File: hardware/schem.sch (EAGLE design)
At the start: 18 parts, among them IC1 7805L, IC2 L298, U2 TINY85-20-DIP

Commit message: Improved ground plane
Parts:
- TINY85: value TINY85-20-DIP -> TINY85
- renumbered U2 to TINY85
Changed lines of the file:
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@@
 <part name="P+4" library="supply1" deviceset="+5V" device=""/>
 <part name="GND2" library="supply1" deviceset="GND" device=""/>
-<part name="U2" library="SparkFun-DigitalIC" deviceset="ATTINY45" device="TINY85-20-DIP" value="TINY85-20-DIP"/>
+<part name="TINY85" library="SparkFun-DigitalIC" deviceset="ATTINY45" device="TINY85-20-DIP" value="TINY85"/>
 <part name="GND4" library="supply1" deviceset="GND" device=""/>
 <part name="P+5" library="supply1" deviceset="+5V" device=""/>
@@
 <instance part="P+4" gate="1" x="180.34" y="106.68"/>
 <instance part="GND2" gate="1" x="165.1" y="86.36"/>
-<instance part="U2" gate="G$1" x="73.66" y="43.18"/>
+<instance part="TINY85" gate="G$1" x="73.66" y="43.18"/>
 <instance part="GND4" gate="1" x="111.76" y="86.36"/>
 <instance part="P+5" gate="1" x="111.76" y="106.68"/>
@@
 </segment>
 <segment>
-<pinref part="U2" gate="G$1" pin="GND"/>
+<pinref part="TINY85" gate="G$1" pin="GND"/>
 <wire x1="58.42" y1="38.1" x2="55.88" y2="38.1" width="0.1524" layer="91"/>
 <wire x1="55.88" y1="38.1" x2="55.88" y2="33.02" width="0.1524" layer="91"/>
@@
 </segment>
 <segment>
-<pinref part="U2" gate="G$1" pin="VCC"/>
+<pinref part="TINY85" gate="G$1" pin="VCC"/>
 <wire x1="58.42" y1="50.8" x2="55.88" y2="50.8" width="0.1524" layer="91"/>
 <wire x1="55.88" y1="50.8" x2="55.88" y2="55.88" width="0.1524" layer="91"/>
@@
 <net name="INP" class="0">
 <segment>
-<pinref part="U2" gate="G$1" pin="PB3(ADC3)"/>
+<pinref part="TINY85" gate="G$1" pin="PB3(ADC3)"/>
 <wire x1="86.36" y1="43.18" x2="88.9" y2="43.18" width="0.1524" layer="91"/>
 <label x="88.9" y="43.18" size="1.778" layer="95"/>
@@
 </segment>
 <segment>
-<pinref part="U2" gate="G$1" pin="PB0(MOSI)"/>
+<pinref part="TINY85" gate="G$1" pin="PB0(MOSI)"/>
 <wire x1="86.36" y1="50.8" x2="88.9" y2="50.8" width="0.1524" layer="91"/>
 <label x="88.9" y="50.8" size="1.778" layer="95"/>
@@
 <net name="MISO" class="0">
 <segment>
-<pinref part="U2" gate="G$1" pin="PB1(MISO)"/>
+<pinref part="TINY85" gate="G$1" pin="PB1(MISO)"/>
 <wire x1="86.36" y1="48.26" x2="88.9" y2="48.26" width="0.1524" layer="91"/>
 <label x="88.9" y="48.26" size="1.778" layer="95"/>
@@
 <net name="RST" class="0">
 <segment>
-<pinref part="U2" gate="G$1" pin="PB5(NRES)"/>
+<pinref part="TINY85" gate="G$1" pin="PB5(NRES)"/>
 <wire x1="86.36" y1="38.1" x2="88.9" y2="38.1" width="0.1524" layer="91"/>
 <label x="88.9" y="38.1" size="1.778" layer="95"/>
@@
 </segment>
 <segment>
-<pinref part="U2" gate="G$1" pin="PB2(SCK/ADC1)"/>
+<pinref part="TINY85" gate="G$1" pin="PB2(SCK/ADC1)"/>
 <wire x1="86.36" y1="45.72" x2="88.9" y2="45.72" width="0.1524" layer="91"/>
 <label x="88.9" y="45.72" size="1.778" layer="95"/>
@@
 <net name="IN2" class="0">
 <segment>
-<pinref part="U2" gate="G$1" pin="PB4(ADC2)"/>
+<pinref part="TINY85" gate="G$1" pin="PB4(ADC2)"/>
 <wire x1="86.36" y1="40.64" x2="88.9" y2="40.64" width="0.1524" layer="91"/>
 <label x="88.9" y="40.64" size="1.778" layer="95"/>

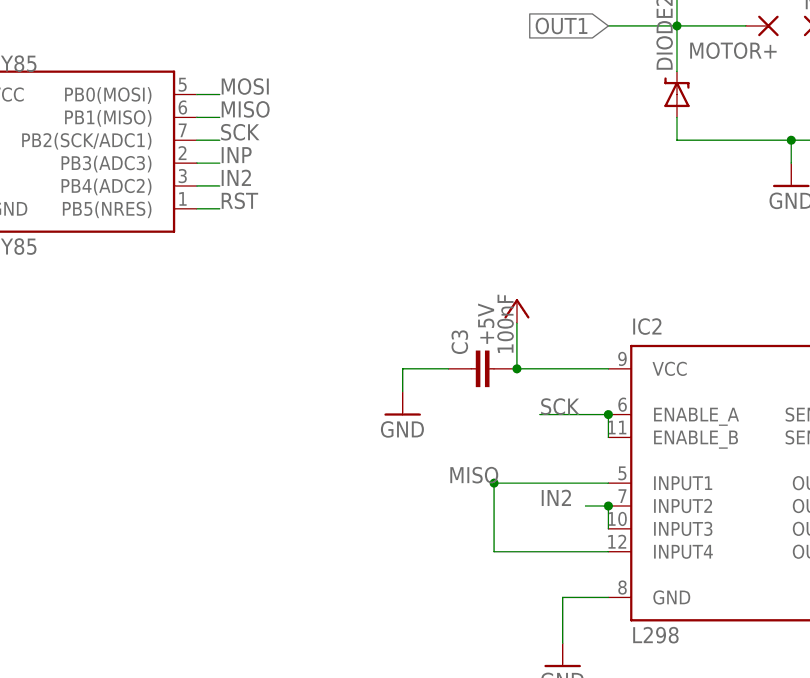
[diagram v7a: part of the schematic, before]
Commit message: switched enable to a pin with PWM output
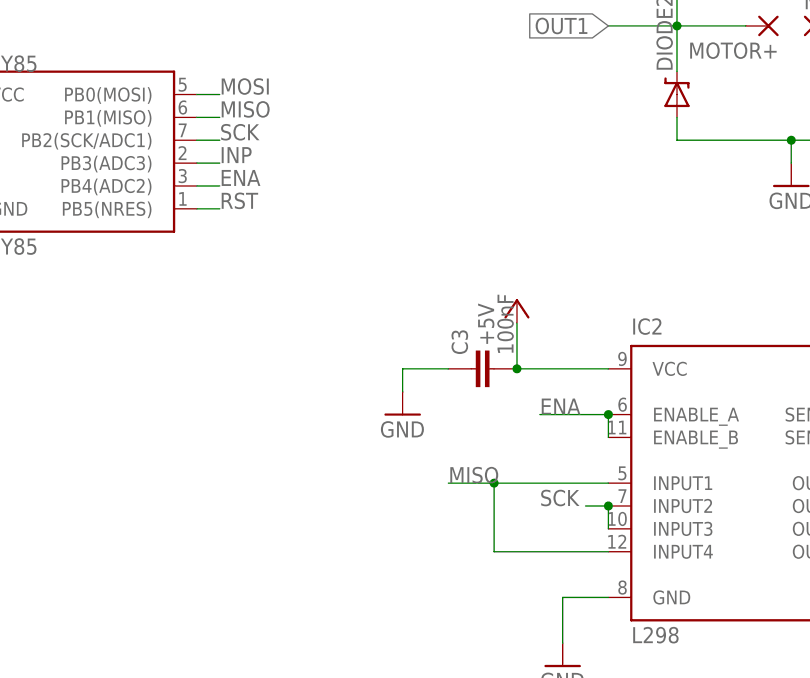
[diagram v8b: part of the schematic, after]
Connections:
- removed net IN2: IC2.INPUT2, IC2.INPUT3, TINY85.PB4(ADC2)
- new net ENA: IC2.ENABLE_A, IC2.ENABLE_B, TINY85.PB4(ADC2)
- net SCK: now also IC2.INPUT2, IC2.INPUT3; no longer IC2.ENABLE_A, IC2.ENABLE_B
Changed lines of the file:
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@@
 <junction x="119.38" y="7.62"/>
 <label x="114.3" y="7.62" size="1.778" layer="95"/>
+<wire x1="119.38" y1="7.62" x2="114.3" y2="7.62" width="0.1524" layer="91"/>
 </segment>
 </net>
@@
 </segment>
 <segment>
-<pinref part="IC2" gate="L298" pin="ENABLE_A"/>
-<pinref part="IC2" gate="L298" pin="ENABLE_B"/>
-<wire x1="132.08" y1="15.24" x2="132.08" y2="12.7" width="0.1524" layer="91"/>
-<wire x1="132.08" y1="15.24" x2="124.46" y2="15.24" width="0.1524" layer="91"/>
-<junction x="132.08" y="15.24"/>
-<label x="124.46" y="15.24" size="1.778" layer="95"/>
+<pinref part="IC2" gate="L298" pin="INPUT3"/>
+<pinref part="IC2" gate="L298" pin="INPUT2"/>
+<wire x1="132.08" y1="2.54" x2="132.08" y2="5.08" width="0.1524" layer="91"/>
+<wire x1="132.08" y1="5.08" x2="129.54" y2="5.08" width="0.1524" layer="91"/>
+<junction x="132.08" y="5.08"/>
+<label x="124.46" y="5.08" size="1.778" layer="95"/>
 </segment>
 </net>
@@
 </segment>
 </net>
-<net name="IN2" class="0">
+<net name="ENA" class="0">
+<segment>
+<pinref part="IC2" gate="L298" pin="ENABLE_A"/>
+<pinref part="IC2" gate="L298" pin="ENABLE_B"/>
+<wire x1="132.08" y1="15.24" x2="132.08" y2="12.7" width="0.1524" layer="91"/>
+<wire x1="132.08" y1="15.24" x2="124.46" y2="15.24" width="0.1524" layer="91"/>
+<junction x="132.08" y="15.24"/>
+<label x="124.46" y="15.24" size="1.778" layer="95"/>
+</segment>
 <segment>
 <pinref part="TINY85" gate="G$1" pin="PB4(ADC2)"/>
@@
 <label x="88.9" y="40.64" size="1.778" layer="95"/>
 </segment>
-<segment>
-<pinref part="IC2" gate="L298" pin="INPUT3"/>
-<pinref part="IC2" gate="L298" pin="INPUT2"/>
-<wire x1="132.08" y1="2.54" x2="132.08" y2="5.08" width="0.1524" layer="91"/>
-<wire x1="132.08" y1="5.08" x2="129.54" y2="5.08" width="0.1524" layer="91"/>
-<junction x="132.08" y="5.08"/>
-<label x="124.46" y="5.08" size="1.778" layer="95"/>
-</segment>
 </net>
